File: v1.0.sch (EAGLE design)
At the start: 251 parts, among them J1 DC-044-A, J2 MICROSD-9P, J3 2p-2.54, J4 2p-2.54, J5 16p-2.54, J6 16p-2.54, J7 2x3p-2.54, J8 2p-2.54, Q2 SSM3J328R,LF, Q3 6pF@32.7680kHz, Q4 BSS138W-7-F, Q5 SSM3J328R,LF, SW1 SW-200D, SW2 SW-200D, SW3 SW-200D, SW4 SW-200D, SW5 SW-200D, SW6 SW-200D, SW7 SW-200D, SW8 SW-200D, U1 MCP23017-E/SO, U10 74HC139N, U11 BZX84C30, U12 SP483ECN-L, U13 FT232RL-SSOP28, U14 FT232RL-SSOP28, U15 FT232RL-SSOP28, U2 MCP79412-I/SN, U3 LOPY, U5 FT232RL-SSOP28, U6 FT232RL-SSOP28, U7 2x14p-2.54, U8 BR24G32-3, Y2 12MHZ

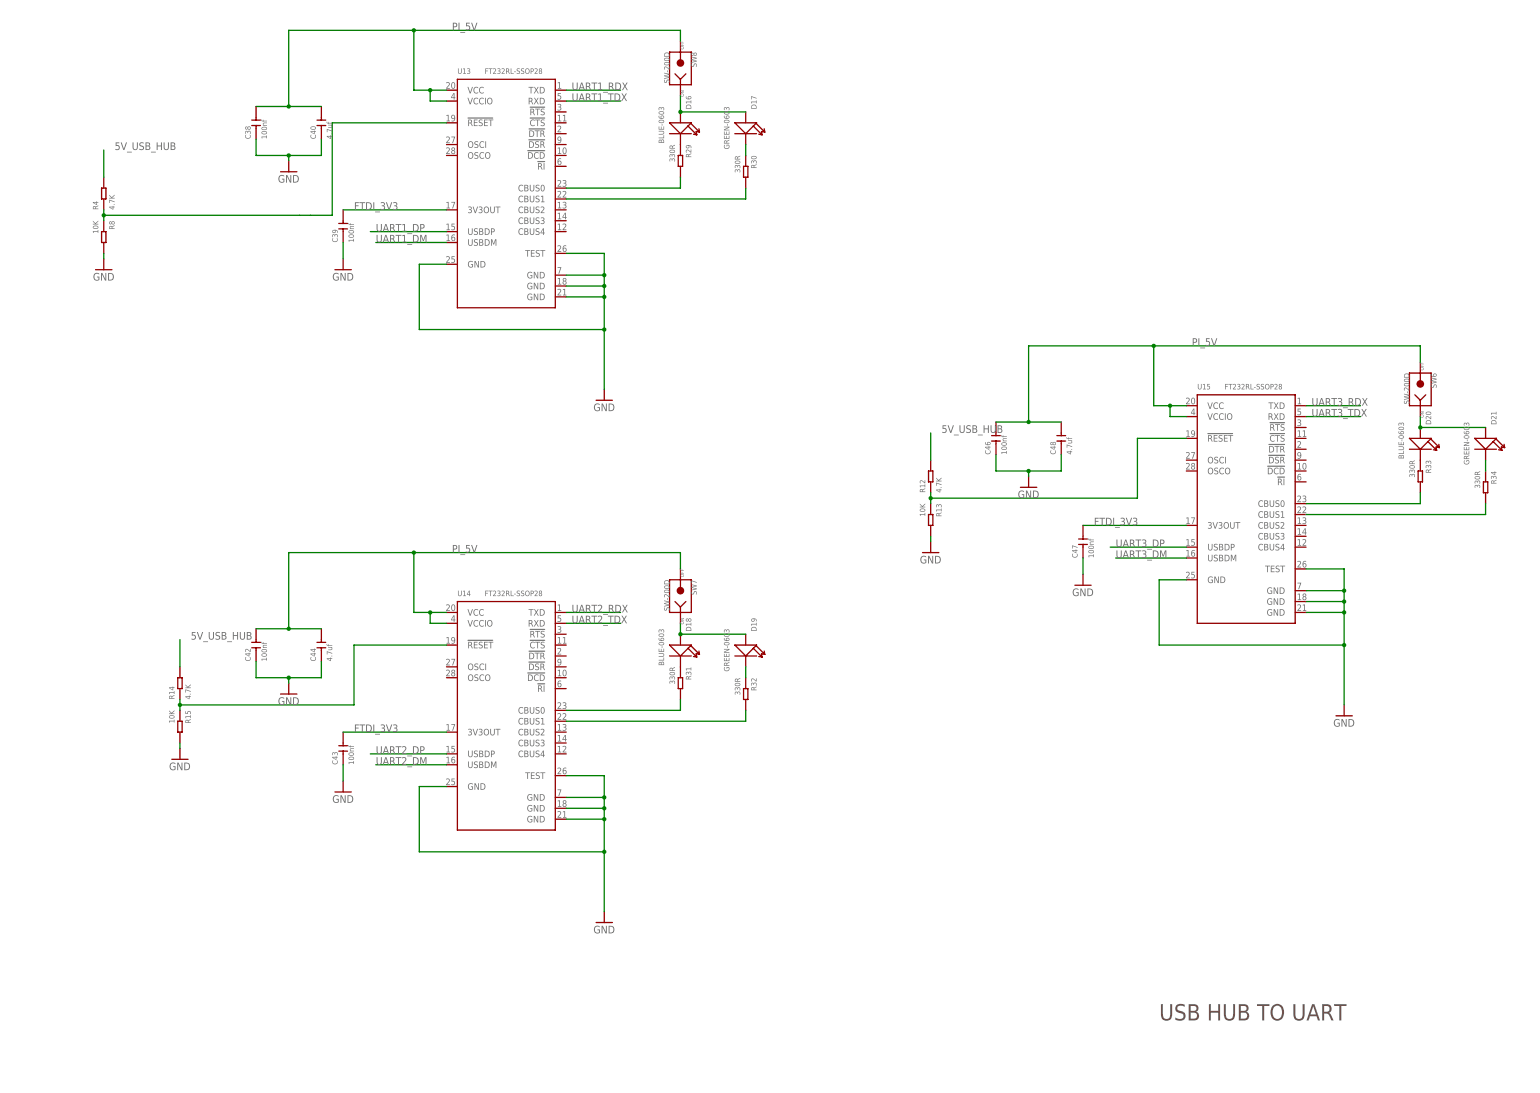
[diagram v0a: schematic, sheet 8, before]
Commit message: adding rs232 level converter
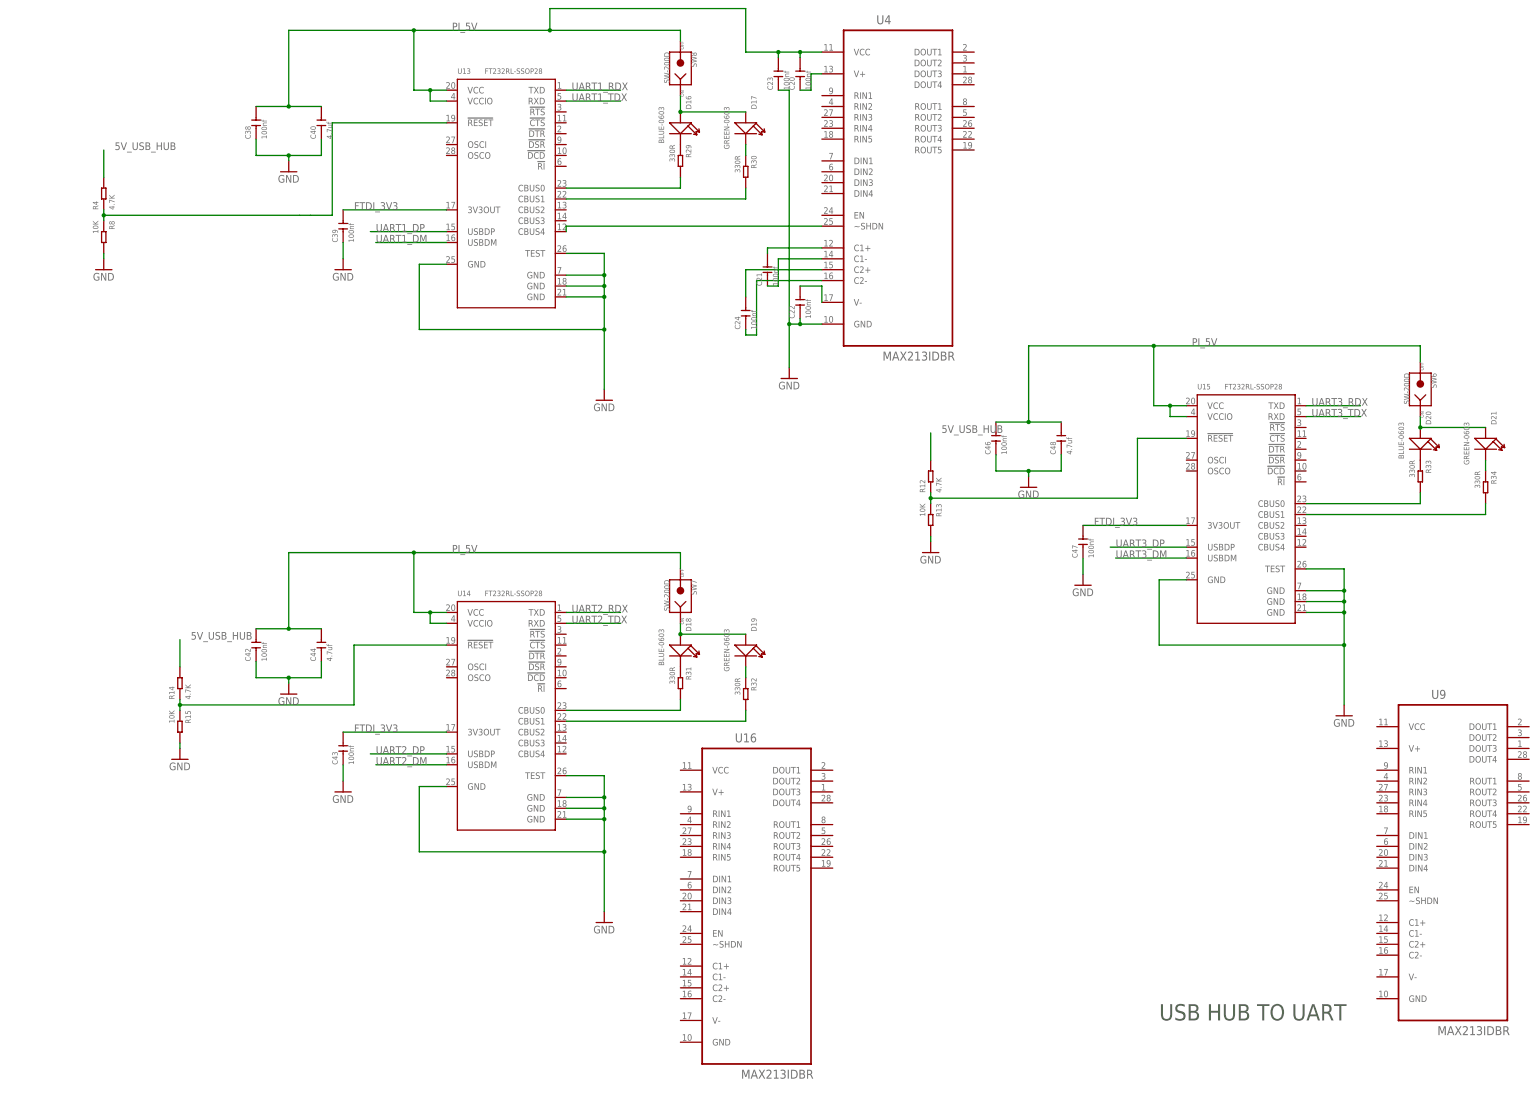
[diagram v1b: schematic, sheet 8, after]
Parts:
- added C20, C21, C22, C23, C24: 100nf, Seeed-Capacitor:CERAMIC-100NF-50V-10%-X7R(0603)
- added U16, U4, U9: MAX213IDBR, ti-max213:MAX213IDBR
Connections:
- new net N$11: C20.1, U4.V+
- new net N$17: C21.2, U4.C1+
- new net N$25: C21.1, U4.C1-
- new net N$28: C22.2, U4.V-
- new net N$38: C24.2, U4.C2+
- new net N$4: U13.CBUS4, U4.~SHDN
- new net N$41: C24.1, U4.C2-
- net GND: now also C22.1, C23.1, U4.GND
- net PI_5V: now also C20.2, C23.2, U4.VCC
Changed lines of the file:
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@@
 <part name="GND41" library="supply1" library_urn="urn:adsk.eagle:library:371" deviceset="GND" device=""/>
 <part name="R16" library="Seeed-Resistor" library_urn="urn:adsk.eagle:library:474" deviceset="SMD-RES-10K-1%-1/10W(0603)" device="" value="10K"/>
+<part name="U4" library="ti-max213" deviceset="MAX213IDBR" device=""/>
+<part name="U9" library="ti-max213" deviceset="MAX213IDBR" device=""/>
+<part name="U16" library="ti-max213" deviceset="MAX213IDBR" device=""/>
+<part name="C20" library="Seeed-Capacitor" library_urn="urn:adsk.eagle:library:464" deviceset="CERAMIC-100NF-50V-10%-X7R(0603)" device="" value="100nf"/>
+<part name="C21" library="Seeed-Capacitor" library_urn="urn:adsk.eagle:library:464" deviceset="CERAMIC-100NF-50V-10%-X7R(0603)" device="" value="100nf"/>
+<part name="C22" library="Seeed-Capacitor" library_urn="urn:adsk.eagle:library:464" deviceset="CERAMIC-100NF-50V-10%-X7R(0603)" device="" value="100nf"/>
+<part name="C23" library="Seeed-Capacitor" library_urn="urn:adsk.eagle:library:464" deviceset="CERAMIC-100NF-50V-10%-X7R(0603)" device="" value="100nf"/>
+<part name="C24" library="Seeed-Capacitor" library_urn="urn:adsk.eagle:library:464" deviceset="CERAMIC-100NF-50V-10%-X7R(0603)" device="" value="100nf"/>
+<part name="GND46" library="supply1" library_urn="urn:adsk.eagle:library:371" deviceset="GND" device=""/>
 </parts>
 <sheets>
@@
 <instance part="Q5" gate="G$1" x="241.3" y="224.79" rot="R90"/>
 <instance part="GND45" gate="1" x="195.58" y="193.04"/>
-<instance part="P+1" gate="1" x="220.98" y="251.46"/>
+<instance part="P+1" gate="1" x="220.98" y="248.92"/>
 <instance part="TP8" gate="G$1" x="58.42" y="233.68"/>
 <instance part="U$5" gate="G$1" x="101.6" y="226.06"/>
@@
 <wire x1="220.98" y1="242.57" x2="227.33" y2="242.57" width="0.1524" layer="91"/>
 <wire x1="227.33" y1="242.57" x2="227.33" y2="234.95" width="0.1524" layer="91"/>
-<wire x1="220.98" y1="242.57" x2="220.98" y2="248.92" width="0.1524" layer="91"/>
+<wire x1="220.98" y1="242.57" x2="220.98" y2="246.38" width="0.1524" layer="91"/>
 <junction x="220.98" y="242.57"/>
 <pinref part="P+1" gate="1" pin="+5V"/>
@@
 <instance part="SW7" gate="G$1" x="294.64" y="165.1" rot="R270"/>
 <instance part="SW8" gate="G$1" x="294.64" y="288.29" rot="R270"/>
+<instance part="U4" gate="A" x="345.44" y="264.16"/>
+<instance part="U9" gate="A" x="474.98" y="106.68"/>
+<instance part="U16" gate="A" x="312.42" y="96.52"/>
+<instance part="C20" gate="G$1" x="322.58" y="287.02" rot="R90"/>
+<instance part="C21" gate="G$1" x="314.96" y="241.3" rot="R90"/>
+<instance part="C22" gate="G$1" x="322.58" y="233.68" rot="R90"/>
+<instance part="C23" gate="G$1" x="317.5" y="287.02" rot="R90"/>
+<instance part="C24" gate="G$1" x="309.88" y="231.14" rot="R90"/>
+<instance part="GND46" gate="1" x="320.04" y="215.9"/>
 </instances>
 <busses>
@@
 <pinref part="GND38" gate="1" pin="GND"/>
 </segment>
+<segment>
+<pinref part="U4" gate="A" pin="GND"/>
+<wire x1="327.66" y1="228.6" x2="322.58" y2="228.6" width="0.1524" layer="91"/>
+<wire x1="322.58" y1="228.6" x2="320.04" y2="228.6" width="0.1524" layer="91"/>
+<wire x1="320.04" y1="228.6" x2="320.04" y2="218.44" width="0.1524" layer="91"/>
+<pinref part="GND46" gate="1" pin="GND"/>
+<pinref part="C23" gate="G$1" pin="1"/>
+<wire x1="317.5" y1="283.21" x2="320.04" y2="283.21" width="0.1524" layer="91"/>
+<wire x1="320.04" y1="283.21" x2="320.04" y2="228.6" width="0.1524" layer="91"/>
+<junction x="320.04" y="228.6"/>
+<pinref part="C22" gate="G$1" pin="1"/>
+<wire x1="322.58" y1="229.87" x2="322.58" y2="228.6" width="0.1524" layer="91"/>
+<junction x="322.58" y="228.6"/>
+</segment>
 </net>
 <net name="N$100" class="0">
@@
 <wire x1="236.22" y1="280.67" x2="236.22" y2="283.21" width="0.1524" layer="91"/>
 <junction x="236.22" y="283.21"/>
-<wire x1="232.41" y1="297.18" x2="294.64" y2="297.18" width="0.1524" layer="91"/>
+<wire x1="232.41" y1="297.18" x2="264.16" y2="297.18" width="0.1524" layer="91"/>
 <label x="241.3" y="297.18" size="1.778" layer="95"/>
 <pinref part="C40" gate="G$1" pin="2"/>
 <pinref part="C38" gate="G$1" pin="2"/>
+<wire x1="264.16" y1="297.18" x2="294.64" y2="297.18" width="0.1524" layer="91"/>
 <wire x1="210.82" y1="279.4" x2="203.2" y2="279.4" width="0.1524" layer="91"/>
 <wire x1="203.2" y1="279.4" x2="195.58" y2="279.4" width="0.1524" layer="91"/>
@@
 <pinref part="SW8" gate="G$1" pin="2"/>
 <wire x1="294.64" y1="294.64" x2="294.64" y2="297.18" width="0.1524" layer="91"/>
+<wire x1="264.16" y1="297.18" x2="264.16" y2="302.26" width="0.1524" layer="91"/>
+<junction x="264.16" y="297.18"/>
+<wire x1="264.16" y1="302.26" x2="309.88" y2="302.26" width="0.1524" layer="91"/>
+<wire x1="309.88" y1="302.26" x2="309.88" y2="292.1" width="0.1524" layer="91"/>
+<pinref part="U4" gate="A" pin="VCC"/>
+<wire x1="309.88" y1="292.1" x2="317.5" y2="292.1" width="0.1524" layer="91"/>
+<pinref part="C23" gate="G$1" pin="2"/>
+<wire x1="317.5" y1="292.1" x2="322.58" y2="292.1" width="0.1524" layer="91"/>
+<wire x1="322.58" y1="292.1" x2="327.66" y2="292.1" width="0.1524" layer="91"/>
+<wire x1="317.5" y1="290.83" x2="317.5" y2="292.1" width="0.1524" layer="91"/>
+<junction x="317.5" y="292.1"/>
+<pinref part="C20" gate="G$1" pin="2"/>
+<wire x1="322.58" y1="290.83" x2="322.58" y2="292.1" width="0.1524" layer="91"/>
+<junction x="322.58" y="292.1"/>
 </segment>
 <segment>
@@
 </segment>
 </net>
+<net name="N$11" class="0">
+<segment>
+<pinref part="U4" gate="A" pin="V+"/>
+<wire x1="327.66" y1="287.02" x2="325.12" y2="287.02" width="0.1524" layer="91"/>
+<wire x1="325.12" y1="287.02" x2="325.12" y2="283.21" width="0.1524" layer="91"/>
+<pinref part="C20" gate="G$1" pin="1"/>
+<wire x1="322.58" y1="283.21" x2="325.12" y2="283.21" width="0.1524" layer="91"/>
+</segment>
+</net>
+<net name="N$17" class="0">
+<segment>
+<pinref part="U4" gate="A" pin="C1+"/>
+<pinref part="C21" gate="G$1" pin="2"/>
+<wire x1="327.66" y1="246.38" x2="314.96" y2="246.38" width="0.1524" layer="91"/>
+<wire x1="314.96" y1="246.38" x2="314.96" y2="245.11" width="0.1524" layer="91"/>
+</segment>
+</net>
+<net name="N$25" class="0">
+<segment>
+<pinref part="C21" gate="G$1" pin="1"/>
+<wire x1="314.96" y1="237.49" x2="317.5" y2="237.49" width="0.1524" layer="91"/>
+<wire x1="317.5" y1="237.49" x2="317.5" y2="243.84" width="0.1524" layer="91"/>
+<pinref part="U4" gate="A" pin="C1-"/>
+<wire x1="317.5" y1="243.84" x2="327.66" y2="243.84" width="0.1524" layer="91"/>
+</segment>
+</net>
+<net name="N$28" class="0">
+<segment>
+<pinref part="C22" gate="G$1" pin="2"/>
+<pinref part="U4" gate="A" pin="V-"/>
+<wire x1="322.58" y1="237.49" x2="327.66" y2="237.49" width="0.1524" layer="91"/>
+<wire x1="327.66" y1="237.49" x2="327.66" y2="233.68" width="0.1524" layer="91"/>
+</segment>
+</net>
+<net name="N$38" class="0">
+<segment>
+<pinref part="U4" gate="A" pin="C2+"/>
+<pinref part="C24" gate="G$1" pin="2"/>
+<wire x1="327.66" y1="241.3" x2="309.88" y2="241.3" width="0.1524" layer="91"/>
+<wire x1="309.88" y1="241.3" x2="309.88" y2="234.95" width="0.1524" layer="91"/>
+</segment>
+</net>
+<net name="N$41" class="0">
+<segment>
+<pinref part="U4" gate="A" pin="C2-"/>
+<wire x1="327.66" y1="238.76" x2="312.42" y2="238.76" width="0.1524" layer="91"/>
+<wire x1="312.42" y1="238.76" x2="312.42" y2="226.06" width="0.1524" layer="91"/>
+<pinref part="C24" gate="G$1" pin="1"/>
+<wire x1="312.42" y1="226.06" x2="309.88" y2="226.06" width="0.1524" layer="91"/>
+<wire x1="309.88" y1="226.06" x2="309.88" y2="227.33" width="0.1524" layer="91"/>
+</segment>
+</net>
+<net name="N$4" class="0">
+<segment>
+<pinref part="U4" gate="A" pin="~SHDN"/>
+<pinref part="U13" gate="1" pin="CBUS4"/>
+<wire x1="327.66" y1="251.46" x2="267.97" y2="251.46" width="0.1524" layer="91"/>
+<wire x1="267.97" y1="251.46" x2="267.97" y2="250.19" width="0.1524" layer="91"/>
+</segment>
+</net>
